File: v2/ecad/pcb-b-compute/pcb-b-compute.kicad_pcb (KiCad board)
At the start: 4 copper layers, 245 x 170 mm, 164 parts, among them Q1 2N7002 (SOT-23) OnOff open-dr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, U1 FE1.1s, U10 TPS22810DRV, U11 INA219AIDCN, U12 USBLC6-2SC6, U13 TPS22810DRV, U14 INA219AIDCN, U15 TPS22810DRV, U16 INA219AIDCN, U17 USBLC6-2SC6, U2 USBLC6-2SC6, U20 PCA9555PW, U3 USBLC6-2SC6, U4 TPS2065CDBV, U5 INA219AIDCN, U6 USBLC6-2SC6, U7 TPS2065CDBV, U8 INA219AIDCN, U9 USBLC6-2SC6, Y1 12 MHz 3225

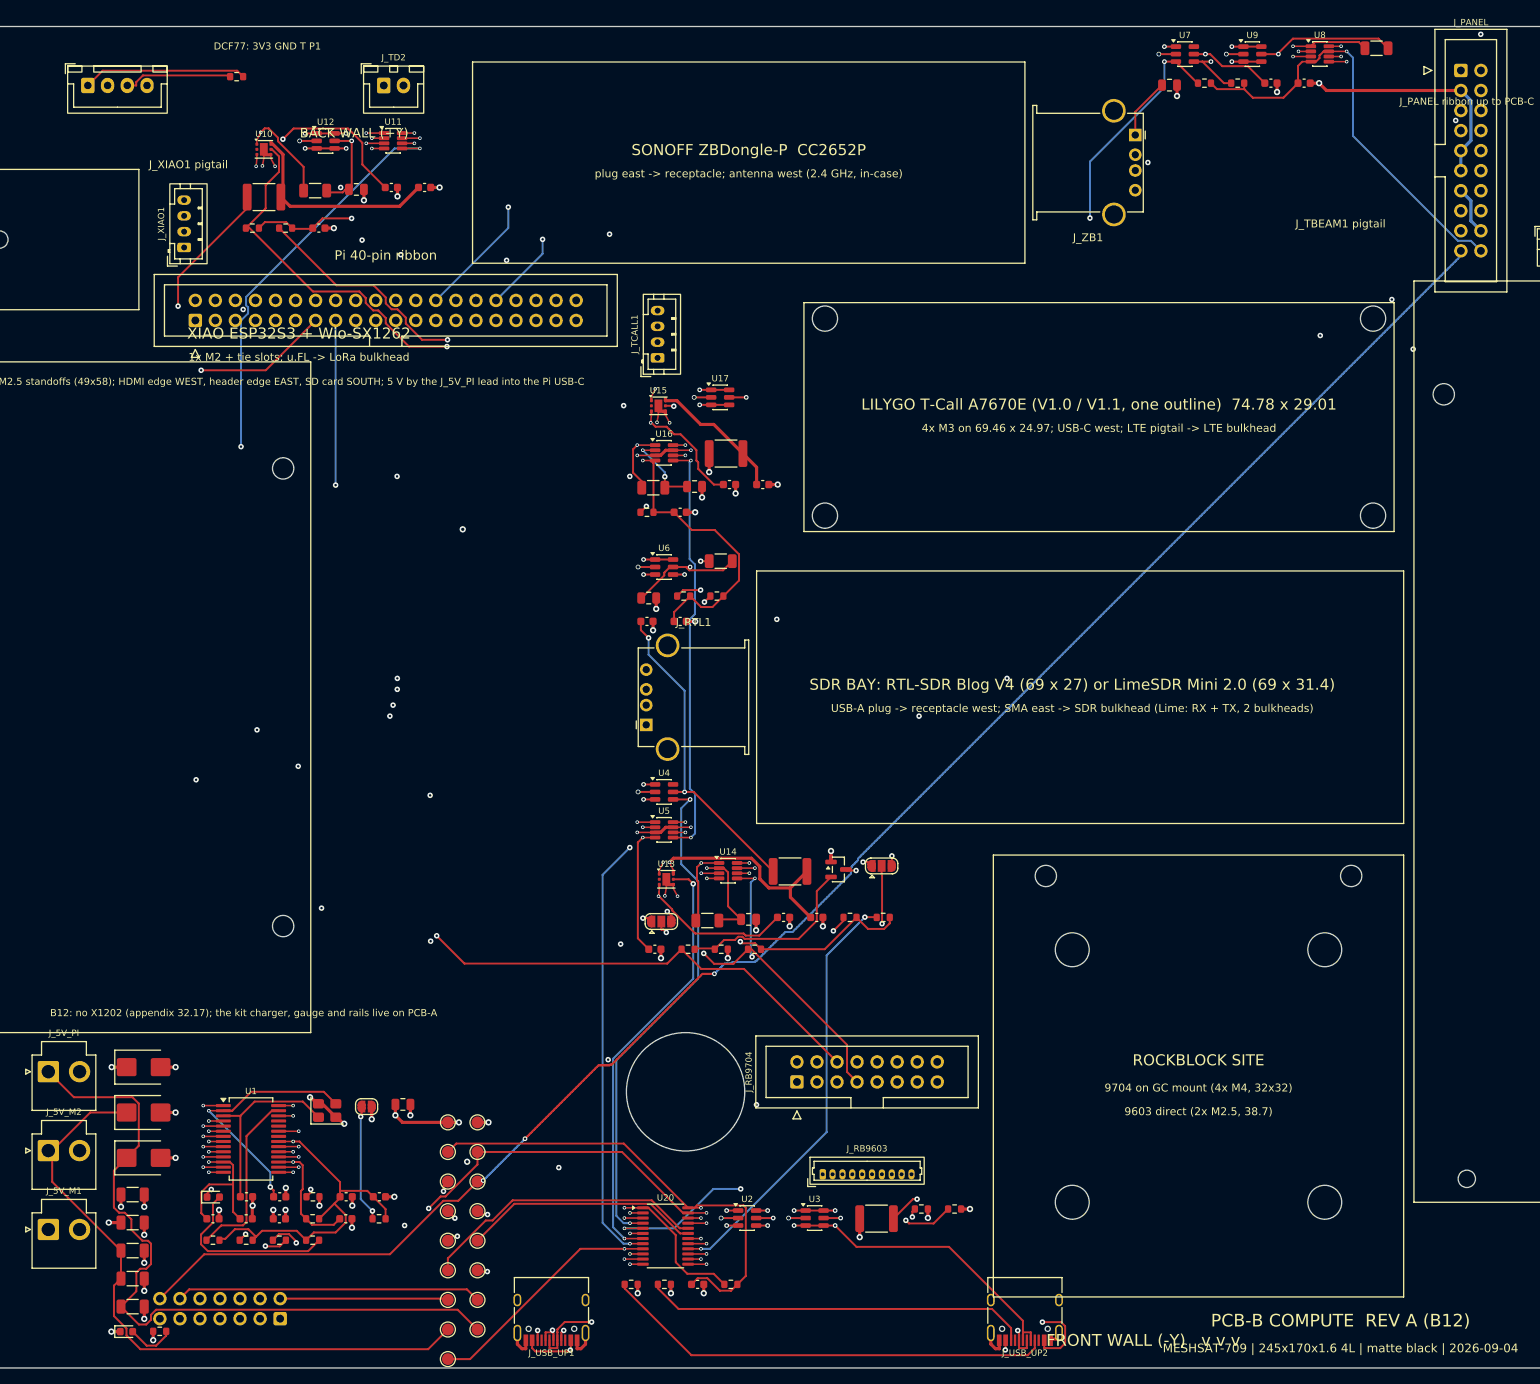
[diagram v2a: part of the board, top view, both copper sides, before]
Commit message: feat(release): A19, B12, E4 and E5 deliverables, all 0 hard and 0 unrouted; battery module model [MESHSAT-789] [MESHSAT-790] [MESHSAT-791]
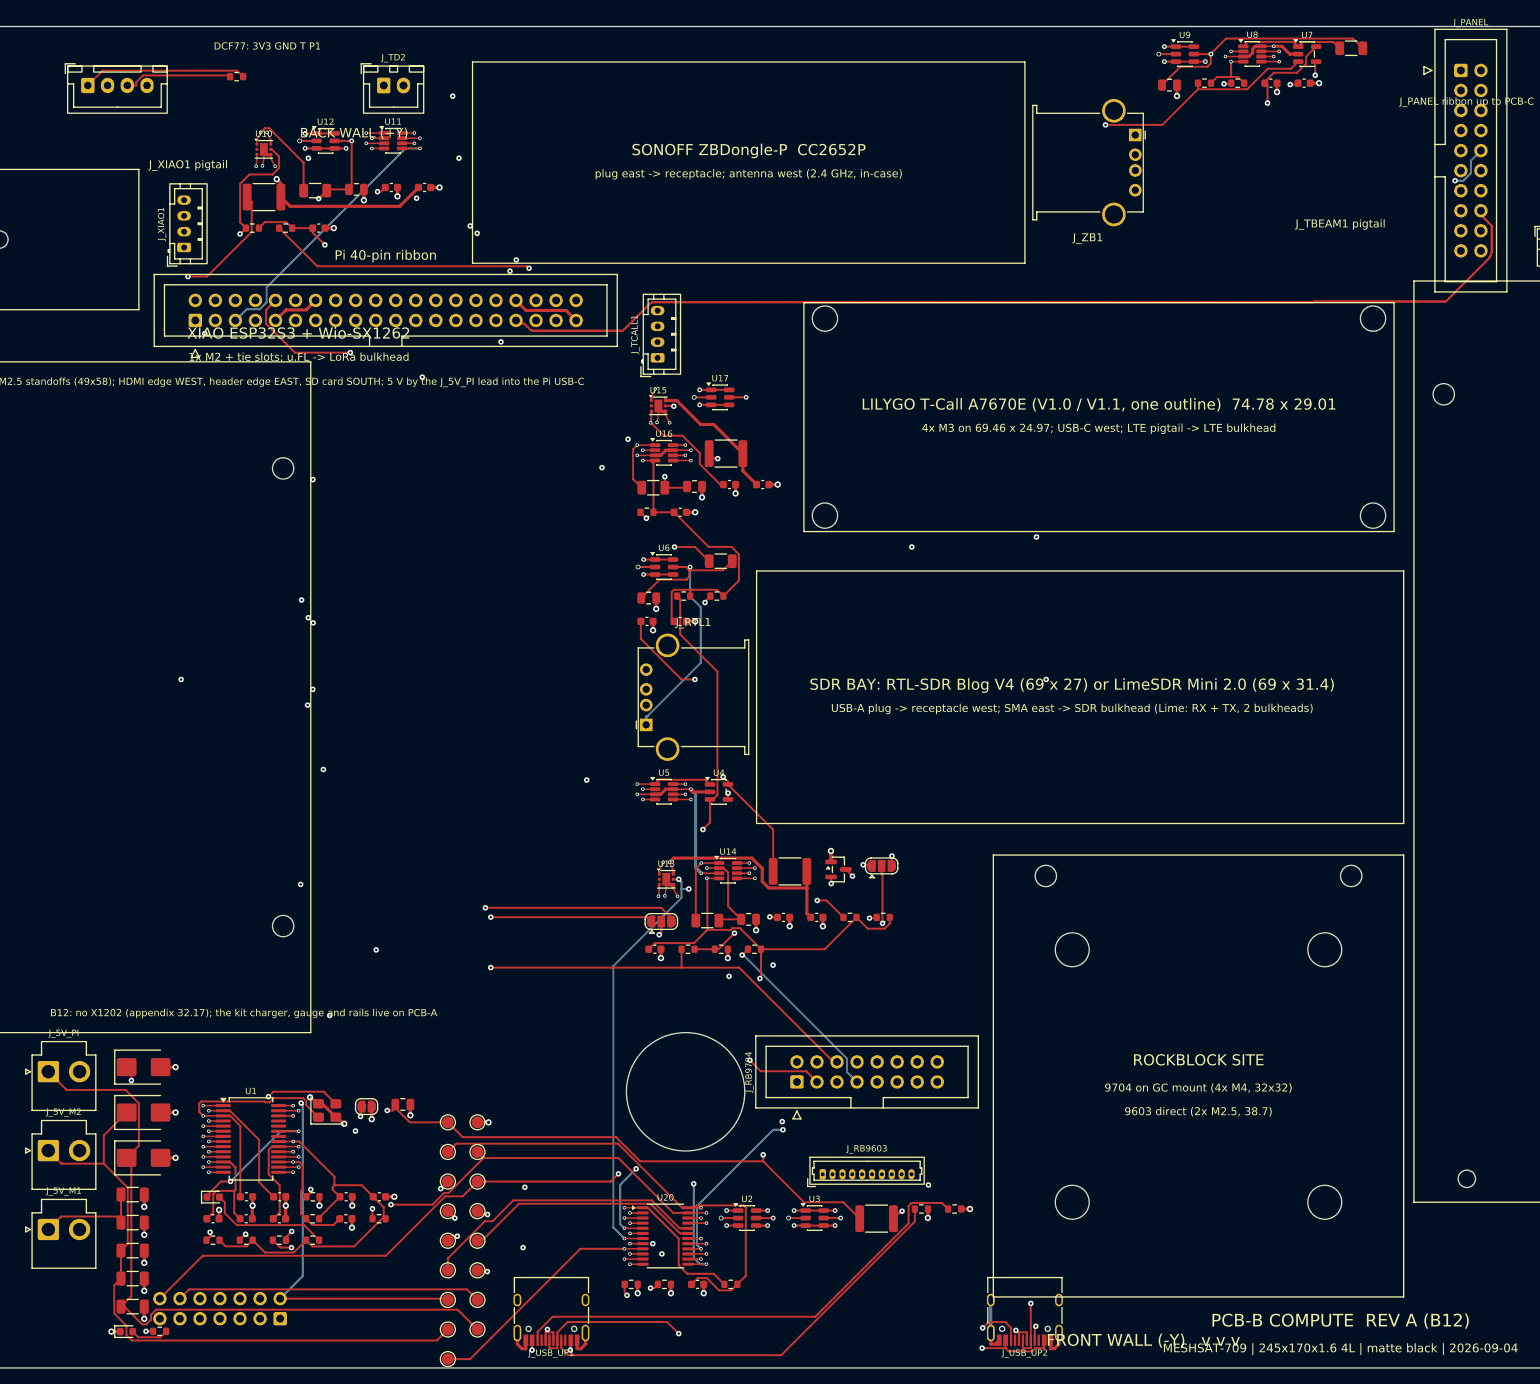
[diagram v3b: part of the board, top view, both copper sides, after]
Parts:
- C3, C4: value 22p -> 33p
- TP1: value +5V -> +5V_M1
- U4, U7: footprint SOT-23-6 -> SOT-23-5
- moved U7 15.5 mm to (215.8, 28.5)
- moved U8 8.55 mm to (208.8, 28.5)
- moved U9 8.55 mm to (200.3, 28.5)
- moved U4 6.95 mm to (141.2, 122.0)
- moved U5 4.83 mm to (134.3, 122.0)
- moved R16 3.20 mm to (221.4, 27.8)
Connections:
- net +5V renamed /+5V_M1
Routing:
- net GND: track 1029.5 -> 971.9 mm, vias 76 -> 73
- net /TX_INHIBIT_n: track 219.1 -> 250.9 mm, vias 3 -> 2
- net /SDA: track 460.8 -> 434.2 mm, vias 8 -> 11
- net /VBUS_A_SENSE: track 153.9 -> 127.4 mm, vias 3 -> 2
- net /EN_XIAO: track 168.7 -> 192.7 mm, vias 2 -> 3
- net /RB_XMTG: track 138.0 -> 161.9 mm
- net /USB_ZB_N: track 243.6 -> 263.7 mm
- net /EXP_INT: track 353.4 -> 372.8 mm
- net /USB_TC_P: track 169.7 -> 151.8 mm, vias 4 -> 3
- net /+5V_M1: track 361.2 -> 343.7 mm, vias 12 -> 6
- net /EN_RTL: track 91.2 -> 106.4 mm, vias 3 -> 4
- net /RB_NETAV: track 158.1 -> 173.0 mm, vias 2 -> 1
- net /SW_ZB: track 27.9 -> 13.3 mm, vias 2 -> 0
- net /+5V_M2: track 446.2 -> 460.3 mm, vias 5 -> 6
- net /USB_ZB_P: track 241.2 -> 255.1 mm
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- added copper zone on In2.Cu, net +5V_M1
- removed copper zone on In2.Cu, net /+5V_M1

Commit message: feat(ecad): A19 rerouted on locked fine-pitch escapes (0 open, 0 hard), B12, E4 and E5 finished on real-net planes [MESHSAT-709] [MESHSAT-789]
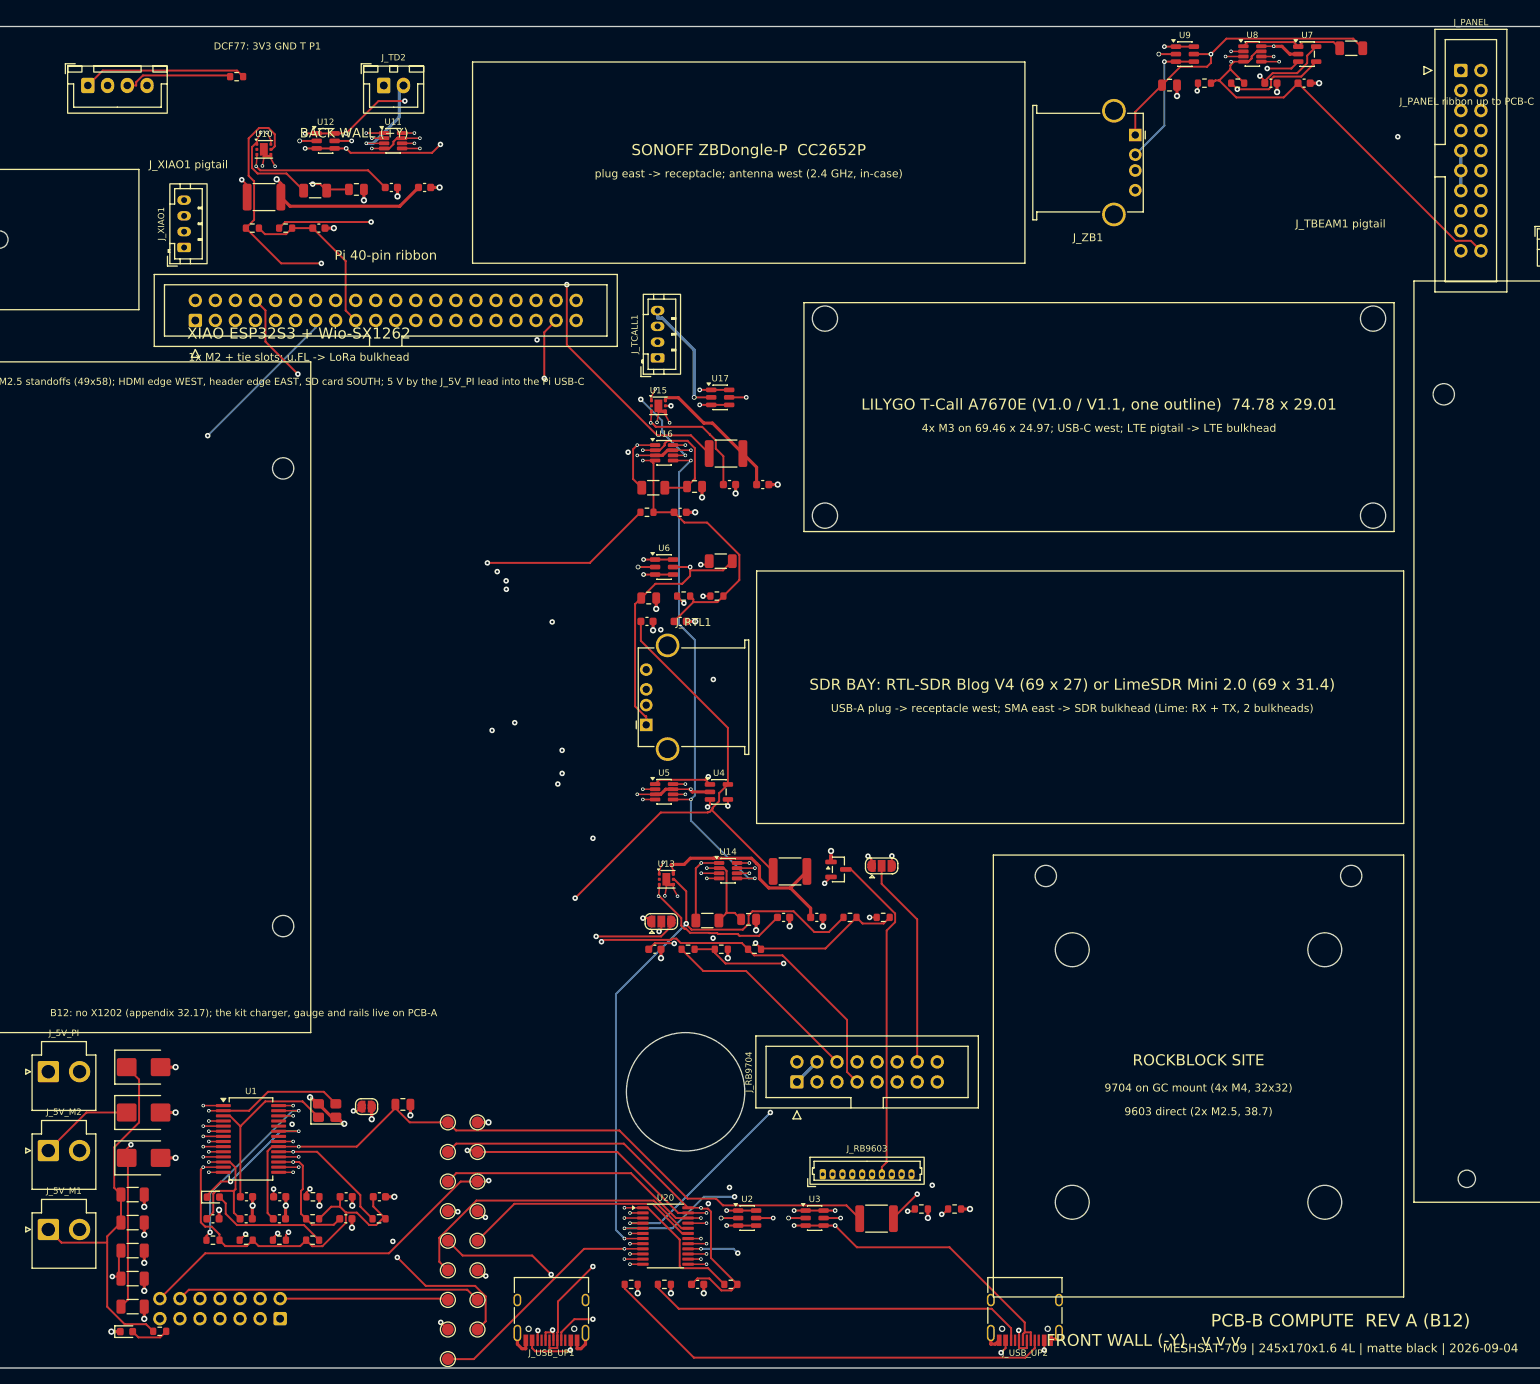
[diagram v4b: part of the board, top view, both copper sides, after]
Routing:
- net /USB_ZB_N: track 263.7 -> 205.6 mm, vias 5 -> 4
- net /+5V_M1: track 343.7 -> 398.8 mm, vias 6 -> 2
- net /USB_ZB_P: track 255.1 -> 204.4 mm
- net +3V3: track 612.3 -> 567.6 mm, vias 14 -> 11
- net /UART2_TX: track 149.1 -> 109.9 mm
- net /+5V_M2: track 460.3 -> 496.2 mm, vias 6 -> 5
- net /RB_NETAV: track 173.0 -> 139.7 mm
- net /SCL: track 424.7 -> 451.8 mm
- net /UART0_TX: track 141.8 -> 115.3 mm
- net /USB_RTL_P: track 132.5 -> 107.3 mm
- net /USB_RTL_N: track 127.9 -> 103.5 mm
- net /EN_TC: track 127.5 -> 150.7 mm, vias 4 -> 3
- net /RB_CTRL: track 143.9 -> 166.4 mm, vias 1 -> 0
- net /EN_XIAO: track 192.7 -> 171.1 mm, vias 3 -> 2
- net /PI_KILL: track 149.7 -> 169.2 mm
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- added copper zone on In2.Cu, net /+5V_M1
- removed copper zone on In2.Cu, net +5V_M1

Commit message: feat(pcb-b): B13 routed and finished on the laptop [MESHSAT-795]
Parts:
- removed C20: 1n, C_0603_1608Metric
- removed C21: 100n, C_0603_1608Metric
- removed C22: 10u, C_0805_2012Metric
- removed C29: 1u, C_0603_1608Metric
- removed F2, F4: 2A hold 1812, Fuse_1812_4532Metric
- removed H15: M2.5 standoff, T-Beam 1W, MountingHole_2.7mm_M2.5
- removed H16, H17: M2 standoff, T-Beam 1W, MountingHole_2.2mm_M2
- removed H18: M2 standoff, Wio-SX1262, MountingHole_2.2mm_M2
- removed H19, H20, H21, H22: M4, GC 9704 bracket, MountingHole_4.3mm_M4
- removed H23, H24: M2.5, RockBLOCK 9603, MountingHole_2.7mm_M2.5
- removed JP1: BUSJ to GND = bus-powered, SolderJumper-2_P1.3mm_Open_RoundedPad1.0x1.5mm
- removed JP3: UART TX select: A=UART2 (BCM4) B=UART0 (BCM14), SolderJumper-3_P1.3mm_Open_RoundedPad1.0x1.5mm
- removed JP4: UART RX select: A=UART2 (BCM5) B=UART0 (BCM15), SolderJumper-3_P1.3mm_Open_RoundedPad1.0x1.5mm
- removed J_GPIO1: Pi 5 GPIO ribbon 2x20, IDC-Header_2x20_P2.54mm_Vertical
- removed J_TBEAM1, J_TCALL1, J_XIAO1: USB-C pigtail header (JST-PH 2.0): VBUS D- D+ GND, JST_PH_B4B-PH-K_1x04_P2.00mm_Vertical
- removed J_USB_UP1, J_USB_UP2: USB-C 2.0 receptacle, USB_C_Receptacle_HRO_TYPE-C-31-M-12
- removed J_ZB1: USB-A receptacle ZigBee, USB_A_Stewart_SS-52100-001_Horizontal
- removed R10, R11, R12, R9: 5.1k, R_0603_1608Metric
- removed R15, R17, R20: 10k, R_0603_1608Metric
- removed R16: 0.1R 1% 1206, R_1206_3216Metric
- removed R18, R22: 0.05R 1% 1206, R_1206_3216Metric
- removed R31, R32, R34: 100k, R_0603_1608Metric
- removed S_XIAO1, S_XIAO2, S_ZB1, S_ZB2, S_ZB3, S_ZB4: tie slot, Slot_5x1.8_NPTH
- removed U11, U16: INA219AIDCN, SOT-23-8
- removed U12, U17, U3: USBLC6-2SC6, SOT-23-6
- removed U15: TPS22810DRV, WSON-6-1EP_2x2mm_P0.65mm_EP1x1.6mm
- added BT1: CR2032 holder Keystone 3034 (VBAT, also the NEO-M9N V_BCKP), BatteryHolder_Keystone_3034_1x20mm, F.Cu at (104.0, 83.0)
- added C32: 10u, C_0805_2012Metric, F.Cu at (94.3, 185.0)
- added C35: 100n, C_0603_1608Metric, F.Cu at (110.9, 187.9)
- added C36: 10u, C_0805_2012Metric, F.Cu at (99.0, 185.0)
- added C37: 22u 10V X7R 1210, C_1210_3225Metric, F.Cu at (94.9, 181.2)
- added C38: 22u 10V X7R 1210, C_1210_3225Metric, F.Cu at (100.8, 181.2)
- added C39: 100n, C_0603_1608Metric, F.Cu at (106.7, 190.7)
- added C43: 100u 10V, C_1206_3216Metric, F.Cu at (33.4, 111.8)
- added C44: 100u 10V, C_1206_3216Metric, F.Cu at (33.4, 115.3)
- added C45: 10u, C_0805_2012Metric, F.Cu at (32.8, 118.7)
- added C46: 10u, C_0805_2012Metric, F.Cu at (37.5, 118.7)
- added C47: 10u, C_0805_2012Metric, F.Cu at (32.8, 121.9)
- added C48: 10u, C_0805_2012Metric, F.Cu at (37.5, 121.9)
- added C49: 10u, C_0805_2012Metric, F.Cu at (103.6, 185.0)
- added C50: 100u 6.3V, C_1206_3216Metric, F.Cu at (102.3, 60.8)
- added C51: 100n, C_0603_1608Metric, F.Cu at (111.5, 60.4)
- added C52: 33p, C_0402_1005Metric, F.Cu at (100.2, 70.0)
- added C53: 10p, C_0402_1005Metric, F.Cu at (103.2, 70.0)
- added C54: 100n, C_0603_1608Metric, F.Cu at (47.6, 160.5)
- added C55: 100n, C_0603_1608Metric, F.Cu at (32.6, 165.3)
- added C56: 33p, C_0402_1005Metric, F.Cu at (106.3, 70.0)
- added C57: 33p, C_0402_1005Metric, F.Cu at (109.4, 70.0)
- added C58: 33p, C_0402_1005Metric, F.Cu at (112.4, 70.0)
- added C59: 100n, C_0603_1608Metric, F.Cu at (115.8, 60.4)
- added C60: 100n, C_0603_1608Metric, F.Cu at (43.0, 63.1)
- added C61: 10u, C_0805_2012Metric, F.Cu at (34.3, 63.4)
- added C62: 47p, C_0402_1005Metric, F.Cu at (33.5, 66.0)
- added C63: 100n, C_0603_1608Metric, F.Cu at (58.1, 60.3)
- added C64: 10u, C_0805_2012Metric, F.Cu at (71.7, 45.6)
- added C65: 100n, C_0603_1608Metric, F.Cu at (261.4, 89.5)
- added C66: 10u, C_0805_2012Metric, F.Cu at (257.3, 86.6)
- added F7: 0.5A hold 1812, Fuse_1812_4532Metric, F.Cu at (104.1, 169.4)
- added J_DBG: console UART0 (GPIO14/15, 3.3 V): GND TX RX, PinHeader_1x03_P2.54mm_Vertical, F.Cu at (94.4, 148.4)
- added J_DISP: Touch Display 2 FPC 22-pin 0.5 mm (Hirose FH12-22S-0.5SH), 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, Hirose_FH12-22S-0.5SH_1x22-1MP_P0.50mm_Horizontal, F.Cu at (100.0, 101.0)
- added J_FAN: CM5 cooler fan (JST-SH 1.0): 5V GND TACHO PWM; 5 V from the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, JST_SH_BM04B-SRSS-TB_1x04-1MP_P1.00mm_Vertical, F.Cu at (86.0, 76.0)
- added J_FLASH: USB-C 2.0 receptacle, USB_C_Receptacle_HRO_TYPE-C-31-M-12, F.Cu at (120.0, 186.9)
- added J_GNSS1: U.FL to the GNSS bulkhead pigtail, U.FL_Hirose_U.FL-R-SMT-1_Vertical, F.Cu at (50.2, 47.1)
- added J_LTE1: mini PCIe socket 52P H4.0 + 2x M2.5 standoffs: Quectel EG25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, MiniPCIe_Socket_52P_H4.0_Standoff, F.Cu at (124.1, 43.0)
- added J_LTEDBG: EG25-G main UART (3.3 V, bench): GND TX RX, PinHeader_1x03_P2.54mm_Vertical, F.Cu at (96.9, 61.4)
- added J_PMIC: PMIC_Enable: short to force the module off (bench), PinHeader_1x02_P2.54mm_Vertical, F.Cu at (108.8, 148.4)
- added J_PWRBTN: PWR_Button: momentary to GND wakes the module from soft-off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, PinHeader_1x02_P2.54mm_Vertical, F.Cu at (113.6, 148.4)
- added J_RPIBOOT: nRPIBOOT jumper: fit to flash the eMMC over J_FLASH with rp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, PinHeader_1x02_P2.54mm_Vertical, F.Cu at (99.2, 148.4)
- added J_SIM1: nano-SIM push-push GCT SIM8060, nanoSIM_GCT_SIM8060-6-0-14-00, F.Cu at (105.0, 50.2)
- added J_WP: EEPROM_nWP jumper: fit to write-protect the bootloader EEPR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, PinHeader_1x02_P2.54mm_Vertical, F.Cu at (104.0, 148.4)
- added J_ZBDBG: CC2652P cJTAG (bench): 3V3 GND TMSC TCKC RESET, PinHeader_1x05_P2.54mm_Vertical, F.Cu at (257.4, 72.4)
- added L31: 3.3uH XAL4020-332MEB, L_Coilcraft_XAL4020-XXX, F.Cu at (110.7, 169.8)
- added L32: 3.3uH XAL4020-332MEB, L_Coilcraft_XAL4020-XXX, F.Cu at (95.0, 175.9)
- added L40: 27nH 0402 (antenna bias tee), L_0402_1005Metric, F.Cu at (50.8, 62.8)
- added LED3: red ZigBee (DIO_7), LED_0603_1608Metric, F.Cu at (261.8, 86.3)
- added LED4: green ZigBee (DIO_8), LED_0603_1608Metric, F.Cu at (257.1, 89.6)
- added LED5: green ACT (LED_nACT sinks), LED_0603_1608Metric, F.Cu at (123.2, 147.4)
- added LED6: red PWR, LED_0603_1608Metric, F.Cu at (94.1, 157.3)
- added Q2: BC857: LED_nPWR must be buffered (datasheet Table 4), SOT-23, F.Cu at (118.5, 148.3)
- added Q3: 2N7002, SOT-23, F.Cu at (75.2, 162.1)
- added Q4: 2N7002, SOT-23, F.Cu at (80.3, 162.1)
- added Q5: 2N7002, SOT-23, F.Cu at (85.4, 162.1)
- added R35: 33.2k 1%, R_0603_1608Metric, F.Cu at (94.1, 187.9)
- added R36: 10k 1%, R_0603_1608Metric, F.Cu at (98.3, 187.9)
- added R37: 100k, R_0603_1608Metric, F.Cu at (102.5, 187.9)
- added R38: 100k, R_0603_1608Metric, F.Cu at (106.7, 187.9)
- added R39: 33.2k 1%, R_0603_1608Metric, F.Cu at (94.1, 190.7)
- added R40: 10k 1%, R_0603_1608Metric, F.Cu at (98.3, 190.7)
- added R41: 0.05R 1% 1206, R_1206_3216Metric, F.Cu at (106.6, 180.7)
- added R42: 100k, R_0603_1608Metric, F.Cu at (102.5, 190.7)
- added R46: 1k, R_0603_1608Metric, F.Cu at (98.4, 157.2)
- added R47: 10k, R_0603_1608Metric, F.Cu at (102.6, 157.2)
- added R48: 1k, R_0603_1608Metric, F.Cu at (106.8, 157.2)
- added R49: 10k, R_0603_1608Metric, F.Cu at (111.0, 157.2)
- added R50: 5.1k, R_0603_1608Metric, F.Cu at (128.1, 182.2)
- added R51: 5.1k, R_0603_1608Metric, F.Cu at (132.3, 182.2)
- added R52: 10k, R_0603_1608Metric, F.Cu at (80.4, 170.4)
- added R53: 10k, R_0603_1608Metric, F.Cu at (84.6, 170.4)
- added R54: 10k, R_0603_1608Metric, F.Cu at (66.1, 174.0)
- added R55: 4.7k, R_0603_1608Metric, F.Cu at (70.3, 174.0)
- added R56: 10k, R_0603_1608Metric, F.Cu at (43.4, 160.5)
- added R57: 2.2k, R_0603_1608Metric, F.Cu at (36.8, 165.3)
- added R58: 2.2k, R_0603_1608Metric, F.Cu at (41.0, 165.3)
- added R59: 4.7k, R_0603_1608Metric, F.Cu at (120.0, 60.4)
- added R60: 4.7k, R_0603_1608Metric, F.Cu at (124.2, 60.4)
- added R61: 10k, R_0603_1608Metric, F.Cu at (128.4, 60.4)
- added R62: 10k, R_0603_1608Metric, F.Cu at (88.1, 70.2)
- added R63: 10k, R_0603_1608Metric, F.Cu at (92.3, 70.2)
- added R64: 1k, R_0603_1608Metric, F.Cu at (96.5, 70.2)
- added R65: 10k, R_0603_1608Metric, F.Cu at (38.8, 63.1)
- added R66: 10R, R_0603_1608Metric, F.Cu at (47.2, 63.1)
- added R67: 10k, R_0603_1608Metric, F.Cu at (62.3, 60.3)
- added R68: 10k, R_0603_1608Metric, F.Cu at (265.6, 89.5)
- added R69: 10k, R_0603_1608Metric, F.Cu at (257.1, 92.3)
- added R70: 1k, R_0603_1608Metric, F.Cu at (261.3, 92.3)
- added R71: 1k, R_0603_1608Metric, F.Cu at (265.5, 92.3)
- added TP18: I2S_LRCLK, TestPoint_Pad_D1.5mm, F.Cu at (243.4, 153.1)
- added TP19: VBUS_FLASH, TestPoint_Pad_D1.5mm, F.Cu at (247.1, 153.1)
- added TP20: SDA_CM, TestPoint_Pad_D1.5mm, F.Cu at (250.9, 153.1)
- added TP21: SCL_CM, TestPoint_Pad_D1.5mm, F.Cu at (235.9, 156.9)
- added TP22: +3V3_LTE, TestPoint_Pad_D1.5mm, F.Cu at (239.6, 156.9)
- added TP23: EXP_INT, TestPoint_Pad_D1.5mm, F.Cu at (243.4, 156.9)
- added TP30: EXP_SPARE0, TestPoint_Pad_D1.5mm, F.Cu at (247.1, 156.9)
- added TP31: EXP_SPARE1, TestPoint_Pad_D1.5mm, F.Cu at (250.9, 156.9)
- added TP32: EXP_SPARE2, TestPoint_Pad_D1.5mm, F.Cu at (235.9, 160.6)
- added TP33: EXP_SPARE3, TestPoint_Pad_D1.5mm, F.Cu at (239.6, 160.6)
- added TP34: EXP_SPARE4, TestPoint_Pad_D1.5mm, F.Cu at (243.4, 160.6)
- added TP35: EXP_SPARE5, TestPoint_Pad_D1.5mm, F.Cu at (247.1, 160.6)
- added TP36: EXP_SPARE6, TestPoint_Pad_D1.5mm, F.Cu at (250.9, 160.6)
- added TP37: EXP_SPARE7, TestPoint_Pad_D1.5mm, F.Cu at (235.9, 164.4)
- added TP38: EXP_SPARE8, TestPoint_Pad_D1.5mm, F.Cu at (239.6, 164.4)
- added TP39: EXP_SPARE9, TestPoint_Pad_D1.5mm, F.Cu at (243.4, 164.4)
- added TP40: EXP_SPARE10, TestPoint_Pad_D1.5mm, F.Cu at (247.1, 164.4)
- added U21: PCA9555PW 0x25, TSSOP-24_4.4x7.8mm_P0.65mm, F.Cu at (37.0, 154.3)
- added U30A: Amphenol 10164227-1004A1RLF receptacle A (CM5 pins 1-100, G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, CM5_Conn_A_10164227, F.Cu at (45.0, 112.5)
- added U30B: Amphenol 10164227-1004A1RLF receptacle B (CM5 pins 101-200,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, CM5_Conn_B_10164227, F.Cu at (79.0, 112.5)
- added U31: TPS563201 3.3 V buck from M1 for the board (follows the CM5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, SOT-23-6, F.Cu at (96.3, 164.5)
- added U32: TPS563201 3.3 V buck for the LTE socket (EN_LTE), SOT-23-6, F.Cu at (104.8, 164.5)
- added U33: INA219AIDCN, SOT-23-8, F.Cu at (96.3, 169.3)
- added U34: TCA9517A I2C buffer: A = module (GPIO2/3, +3V3_CM), B = kit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, MSOP-8_3x3mm_P0.65mm, F.Cu at (35.9, 161.5)
- added U40: u-blox NEO-M9N-00B: I2C + PPS, external active antenna, ublox_NEO, F.Cu at (39.8, 52.9)
- added U41: Seeed Wio-SX1262: 1 RF_SW 2 MISO 3 MOSI 4 SCK 5 NRST 6 NSS 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, Seeed_Wio-SX1262, F.Cu at (62.7, 51.5)
- added U42: Ebyte E72-2G4M20S1E CC2652P ZigBee coordinator (ZNP over UA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, Ebyte_E72-2G4M20S1E, F.Cu at (244.4, 76.9)
- C10, C15: value 10u -> 100n; footprint C_0805_2012Metric -> C_0603_1608Metric
- C11, C31, C6, C8: value 1u -> 100n
- C12, C14: value 100n -> 1u
- C13: value 10u -> 1u; footprint C_0805_2012Metric -> C_0603_1608Metric
- C27: value 1n -> 100n
- C3, C4: value 33p -> 27p
- C33, C34: value 100n -> 22u 10V X7R 1210; footprint C_0603_1608Metric -> C_1210_3225Metric
- H10, H11, H12, H9: value M3, T-Call corner -> M4, GC 9704 bracket; footprint MountingHole_3.2mm_M3 -> MountingHole_4.3mm_M4
- H13, H14: value M2.5 standoff, T-Beam 1W -> M2.5, RockBLOCK 9603
- H5, H6, H7, H8: value M2.5 standoff, Pi 5 -> M2.5 standoff 4.0 mm, CM5
- J_5V_M1: value 5 V rail M1 from PCB-A J_5V_M1 (JST-VH, 18 AWG): + - ; hub, display, panel, LTE channel -> 5 V rail M1 from PCB-A J_5V_M1 (JST-VH, 18 AWG): + - ; hub, display, panel, LTE socket, 3.3 V buck
- J_5V_M2: value 5 V rail M2 from PCB-A J_5V_M2 (JST-VH, 18 AWG): + - ; SDR, ZigBee, LoRa, RockBLOCK channels -> 5 V rail M2 from PCB-A J_5V_M2 (JST-VH, 18 AWG): + - ; SDR channel, RockBLOCK channel
- J_5V_PI: value Pi rail 5.1 V 5 A from PCB-A J_5V_PI (JST-VH, 18 AWG): + - ; lead to a USB-C plug in the Pi 5 power input (Rp 10k in th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 -> Pi rail 5.1 V 5 A from PCB-A J_5V_PI (JST-VH, 18 AWG): + - ; the CM5 5 V pins and the fan, no plug
- J_AB1: value A-B interconnect (IDC 2x7, underside) -> A-B interconnect (IDC 2x9, underside); footprint IDC-Header_2x07_P2.54mm_Vertical -> IDC-Header_2x09_P2.54mm_Vertical
- LED2: value amber hub -> amber LTE network (LED_WWAN# sinks)
- Q1: value 2N7002 (SOT-23) OnOff open-drain buffer -> 2N7002 OnOff open-drain buffer
- R2: value 2.7k 1% (REXT, verify datasheet) -> 12.0k 1% (RBIAS)
- R7: value 4.7k -> 10k
- R8: value 1k -> 10k
- TP10: value EXP_SPARE4 -> +3V3_CM
- TP11: value TX_INHIBIT_n -> +1V8_CM
- TP12: value EXP_SPARE5 -> VBUS_EN
- TP13: value PI_KILL -> PMIC_EN
- TP14: value AB_SPARE -> PWR_BUT
- TP15: value +5V_M2 -> GNSS_PPS
- TP16: value +5V_PI -> GNSS_TXD
- TP17: value EXP_SPARE6 -> I2S_BCLK
- TP6: value EXP_SPARE0 -> TX_INHIBIT_n
- TP7: value EXP_SPARE1 -> PI_KILL
- TP8: value EXP_SPARE2 -> +5V_M2
- TP9: value EXP_SPARE3 -> +5V_PI
- U1: value FE1.1s -> USB2517I-JZX seven-port USB 2.0 hub (strap defaults, ports 6-7 disabled); footprint SSOP-28_5.3x10.2mm_P0.65mm -> QFN-64-1EP_9x9mm_P0.5mm_EP4.7x4.7mm
- U10: value TPS22810DRV -> USBLC6-2SC6; footprint WSON-6-1EP_2x2mm_P0.65mm_EP1x1.6mm -> SOT-23-6
- U20: value PCA9555PW -> PCA9555PW 0x20
- U7: value TPS2065CDBV -> USBLC6-2SC6; footprint SOT-23-5 -> SOT-23-6
- U8: value INA219AIDCN -> USBLC6-2SC6; footprint SOT-23-8 -> SOT-23-6
- Y1: value 12 MHz 3225 -> 24 MHz 3225
- moved C34 177.0 mm to (106.8, 175.1)
- moved U9 165.5 mm to (130.3, 178.5)
- moved C14 160.7 mm to (98.7, 142.8)
- moved TP15 149.7 mm to (250.9, 149.4)
- moved TP10 148.7 mm to (250.9, 145.6)
- moved TP5 147.0 mm to (250.9, 141.9)
- moved F6 145.4 mm to (263.4, 72.6)
- moved U7 141.5 mm to (111.8, 124.5)
- moved TP13 141.4 mm to (243.4, 149.4)
- moved TP14 141.4 mm to (247.1, 149.4)
- moved TP8 140.5 mm to (243.4, 145.6)
- moved TP9 140.5 mm to (247.1, 145.6)
- moved C27 139.7 mm to (32.6, 168.0)
- moved TP3 138.9 mm to (243.4, 141.9)
- moved TP4 138.9 mm to (247.1, 141.9)
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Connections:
- C10 pad 1: /+5V_M1 -> +3V3
- C11 pad 1: /HUB_RST -> +3V3
- C12 pad 1: +3V3 -> /HUB_VD18
- C13 pad 1: /5V_RTL -> /HUB_VD18PLL
- C15 pad 1: /5V_ZB -> /+5V_M2
- C17 pad 1: /5V_XIAO -> /5V_RTL
- C27 pad 1: /XIAO_CT -> +3V3
- C31 pad 1: /TC_FUSED -> /BST33
- C31 pad 2: GND -> /SW33
- C33 pad 1: /+5V_M2 -> +3V3
- C34 pad 1: /+5V_M2 -> +3V3
- C5 pad 1: /HUB_VD33 -> +3V3
- C6 pad 1: /HUB_VD33 -> +3V3
- C7 pad 1: /HUB_VD18 -> +3V3
- C8 pad 1: /HUB_VD18 -> +3V3
- C9 pad 1: /+5V_M1 -> +3V3
- J_AB1 pad 11: /VBUS_A_SENSE -> /I2S_BCLK
- J_AB1 pad 12: /AB_SPARE -> /I2S_LRCLK
- J_AB1 pad 4: /USB_A_P -> /USB_WALL_P
- J_AB1 pad 5: /USB_A_N -> /USB_WALL_N
- J_RB9603 pad 1: /UART_RX_M -> /UART2_RX
- J_RB9603 pad 6: /UART_TX_M -> /UART2_TX
- J_RB9704 pad 13: /UART_RX_M -> /UART2_RX
- J_RB9704 pad 14: /UART_TX_M -> /UART2_TX
- LED2 pad 1: /HUB_LED1 -> /LTE_nLED
- LED2 pad 2: /LED_HUB_A -> /LED_LTE_A
- Q1 pad 1: GND -> /Q1_G
- Q1 pad 2: /Q1_G -> GND
- R2 pad 1: /HUB_REXT -> /HUB_RBIAS
- R3 pad 1: /HUB_RST -> /HUB_CFG0
- R3 pad 2: /HUB_VD33 -> GND
- R4 pad 1: /HUB_BUSJ -> /HUB_CFG1
- R4 pad 2: /HUB_VD33 -> GND
- R5 pad 1: /HUB_TESTJ -> /HUB_DIS6M
- R5 pad 2: /HUB_VD33 -> +3V3
- R6 pad 1: /HUB_OVCJ -> /HUB_DIS6P
- R6 pad 2: /HUB_VD33 -> +3V3
- R7 pad 1: /USB_UP_VBUS -> /HUB_DIS7M
- R7 pad 2: /HUB_VBUSM -> +3V3
- R8 pad 1: /HUB_VD33 -> /HUB_DIS7P
- R8 pad 2: /LED_HUB_A -> +3V3
- TP10 pad 1: /EXP_SPARE4 -> /+3V3_CM
- TP11 pad 1: /TX_INHIBIT_n -> /+1V8_CM
- TP12 pad 1: /EXP_SPARE5 -> /VBUS_EN
- TP13 pad 1: /PI_KILL -> /PMIC_EN
- TP14 pad 1: /AB_SPARE -> /PWR_BUT
- TP15 pad 1: /+5V_M2 -> /GNSS_PPS
- TP16 pad 1: /+5V_PI -> /GNSS_TXD
- TP17 pad 1: /EXP_SPARE6 -> /I2S_BCLK
- TP6 pad 1: /EXP_SPARE0 -> /TX_INHIBIT_n
- TP7 pad 1: /EXP_SPARE1 -> /PI_KILL
- TP8 pad 1: /EXP_SPARE2 -> /+5V_M2
- TP9 pad 1: /EXP_SPARE3 -> /+5V_PI
- U1 pad 1: GND -> /USB_RTL_N
- U1 pad 10: /USB_RTL_N -> +3V3
- U1 pad 11: /USB_RTL_P -> (no net)
- U1 pad 12: /HUB_VD18 -> (no net)
- U1 pad 13: /HUB_VD33 -> GND
- U1 pad 14: /HUB_REXT -> (no net)
- U1 pad 15: /USB_UP_N -> (no net)
- U1 pad 16: /USB_UP_P -> (no net)
- U1 pad 17: /HUB_RST -> (no net)
- U1 pad 18: /HUB_VBUSM -> (no net)
- U1 pad 19: /HUB_BUSJ -> GND
- U1 pad 2: /XOUT -> /USB_RTL_P
- U1 pad 20: /+5V_M1 -> (no net)
- U1 pad 21: /HUB_VD33 -> +3V3
- U1 pad 22: (no net) -> +3V3
- U1 pad 23: /HUB_LED1 -> (no net)
- U1 pad 24: (no net) -> +3V3
- U1 pad 25: (no net) -> /HUB_VD18
- U1 pad 26: /HUB_OVCJ -> (no net)
- U1 pad 27: /HUB_TESTJ -> +3V3
- U1 pad 28: /HUB_VD18 -> /FLT_RTL
- U1 pad 3: /XIN -> /USB_WALL_N
- U1 pad 4: /USB_XIAO_N -> /USB_WALL_P
- U1 pad 5: /USB_XIAO_P -> +3V3
- U1 pad 6: /USB_TC_N -> (no net)
- U1 pad 7: /USB_TC_P -> (no net)
- U1 pad 8: /USB_ZB_N -> (no net)
- U1 pad 9: /USB_ZB_P -> (no net)
- U10 pad 1: /SW_XIAO -> /DISP_SDA
- U10 pad 2: (no net) -> GND
- U10 pad 3: /XIAO_CT -> /DISP_SCL
- U10 pad 4: GND -> /DISP_SCL
- U10 pad 5: /EN_XIAO -> /+3V3_CM
- U10 pad 6: /XIAO_FUSED -> /DISP_SDA
- U14 pad 7: /SDA -> /SCL
- U2 pad 5: /USB_UP_VBUS -> +3V3
- U20 pad 10: /EXP_SPARE0 -> /ZB_BSL
- U20 pad 11: /EXP_SPARE1 -> /GNSS_nRST
- U20 pad 14: /FLT_ZB -> /LTE_RI
- U20 pad 15: /FLT_XIAO -> /LTE_WAKE_n
- U20 pad 16: /FLT_RB -> /RB_STATUS
- U20 pad 17: /EXP_SPARE5 -> /RB_NETAV
- U20 pad 18: /EXP_SPARE2 -> /RB_XMTG
- U20 pad 19: /EXP_SPARE3 -> /RB_CTRL
- U20 pad 20: /EXP_SPARE4 -> /RB_IEN
- U20 pad 5: /EN_ZB -> /EN_LTE
- U20 pad 6: /EN_XIAO -> /LTE_W_DIS_n
- U20 pad 7: /EN_RB -> /LTE_PERST_n
- U20 pad 8: /EN_TC -> /LTE_DTR
- U20 pad 9: /EXP_SPARE6 -> /ZB_nRST
- U7 pad 1: /SW_ZB -> /USB_WALL_P
- U7 pad 3: /FLT_ZB -> /USB_WALL_N
- U7 pad 4: /EN_ZB -> /USB_WALL_N
- U7 pad 5: /+5V_M2 -> +3V3
- U8 pad 1: /SW_ZB -> /USB_LTE_P
- U8 pad 2: /5V_ZB -> GND
- U8 pad 3: GND -> /USB_LTE_N
- U8 pad 4: +3V3 -> /USB_LTE_N
- U8 pad 5: /SCL -> /+3V3_LTE
- U8 pad 6: /SDA -> /USB_LTE_P
- U9 pad 1: /USB_ZB_P -> /USB_OTG_P
- U9 pad 3: /USB_ZB_N -> /USB_OTG_N
- U9 pad 4: /USB_ZB_N -> /USB_OTG_N
- U9 pad 5: /5V_ZB -> /VBUS_FLASH
- U9 pad 6: /USB_ZB_P -> /USB_OTG_P
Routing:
- net GND: track 971.5 -> 1831.5 mm, vias 73 -> 171
- net /+3V3_CM: track 0.00 -> 438.1 mm, vias 0 -> 12
- net +3V3: track 567.6 -> 965.0 mm, vias 11 -> 34
- net /+3V3_LTE: track 0.00 -> 393.2 mm, vias 0 -> 9
- net /SDA_CM: track 0.00 -> 362.4 mm, vias 0 -> 9
- net /SCL_CM: track 0.00 -> 334.7 mm, vias 0 -> 8
- net /USB_XIAO_P: track 328.2 -> 0.00 mm, vias 4 -> 0
- net /USB_XIAO_N: track 321.1 -> 0.00 mm, vias 4 -> 0
- net /GNSS_PPS: track 0.00 -> 303.1 mm, vias 0 -> 5
- net /I2S_BCLK: track 0.00 -> 289.1 mm, vias 0 -> 4
- net /+5V_PI: track 94.5 -> 380.5 mm, vias 2 -> 12
- net /GNSS_TXD: track 0.00 -> 274.8 mm, vias 0 -> 4
- net /ZB_nRST: track 0.00 -> 274.4 mm, vias 0 -> 2
- net /I2S_LRCLK: track 0.00 -> 267.9 mm, vias 0 -> 3
- net /ZB_BSL: track 0.00 -> 264.2 mm, vias 0 -> 4
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- added copper zone on F.Cu, net /+5V_PI
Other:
- board text added: "3.3 V BUCKS"
- board text added: "B13: no Pi 5, no ribbon, no USB plug on the compute side (appendix 32.35)"
- board text added: "COMPUTE MODULE 5 on 2x Amphenol 10164227-1004A1RLF (4.0 mm stack), M2.5 x 4 on 33 x 48; CM5 Cooler 41 x 56 over it"
- board text added: "EXPANDERS, I2C BUFFER, LEVEL STAGES"
- board text added: "GNSS NEO-M9N + U.FL -> GPS bulkhead | LoRa Wio-SX1262, IPEX -> LoRa bulkhead"
- board text added: "GPIO connector WEST, high-speed connector EAST; U.FL antenna lead to the WiFi bulkhead (dtparam=ant2)"
- board text added: "J_5V_M1 / J_5V_M2 (VH) from PCB-A; J_5V_PI (VH) beside the module"
- board text added: "J_AB1 2x9 to PCB-A (underside)"
- board text added: "J_FLASH: rpiboot only"
- board text added: "LTE: Quectel EG25-G mini PCIe (full-size card 30 x 50.95) on J_LTE1, 2x M2.5 standoffs; SIM in J_SIM1; pigtails -> LTE bulkhead"
- board text added: "MESHSAT-795 | 245x170x1.6 4L | matte black | 2026-09-04"
- board text added: "USB2517I HUB (upstream = CM5 USB3-0 pair)"
- board text added: "ZIGBEE: Ebyte E72-2G4M20S1E (CC2652P), PCB antenna to the back wall"
- board text removed: "1x M2 + tie slots; u.FL -> LoRa bulkhead"
- board text removed: "4x M3 on 69.46 x 24.97; USB-C west; LTE pigtail -> LTE bulkhead"
- board text removed: "B12: no X1202 (appendix 32.17); the kit charger, gauge and rails live on PCB-A"
- board text removed: "HUB / eFUSE / MONITOR ZONE (phase B2: 4-port USB 2.0 hub, 4x eFuse, INA3221 x2, PCA9554)"
- board text removed: "J_5V_M1 / J_5V_M2 / J_5V_PI (VH): three rails from PCB-A"
- board text removed: "J_AB1 2x7 to PCB-A (underside)"
- board text removed: "J_TBEAM1 pigtail"
- board text removed: "J_USB_UP1"
- board text removed: "J_XIAO1 pigtail"
- board text removed: "J_ZB1"
- board text removed: "LILYGO T-BEAM 1W (alt. LoRa)"
- board text removed: "LILYGO T-Call A7670E (V1.0 / V1.1, one outline) 74.78 x 29.01"
- board text removed: "MESHSAT-709 | 245x170x1.6 4L | matte black | 2026-09-04"
- board text removed: "Pi 40-pin ribbon"
- board text removed: "Pi 5 + cooler on 4x M2.5 standoffs (49x58); HDMI edge WEST, header edge EAST, SD card SOUTH; 5 V by the J_5V_PI lead into the Pi USB-C"
- board text removed: "SMA"
- board text removed: "SONOFF ZBDongle-P CC2652P"
- board text removed: "USB-C"
- board text removed: "XIAO ESP32S3 + Wio-SX1262"
- board text removed: "bare PCB + fan, 5 standoffs 6 mm; SMA N (right-angle plug); USB-C W"
- board text removed: "plug east -> receptacle; antenna west (2.4 GHz, in-case)"

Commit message: fix(pcb-b): B13 project board after the reordered finish [MESHSAT-795]
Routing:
- net /SDA: track 423.1 -> 438.2 mm, vias 7 -> 8
- net /5V_RTL: track 49.9 -> 50.5 mm
